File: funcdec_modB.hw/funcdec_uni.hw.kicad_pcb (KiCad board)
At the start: 2 copper layers, 32 x 17.5 mm, 27 parts, among them J1 Track2, J2 Track1, J3 PROG, J4 Functions, Q1 BSS138, Q2 AP2626, Q3 AP2626, Q4 AP2626, U1 AP2204K-5.0, U2 ATtiny1614-SS

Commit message: ack circuit correction
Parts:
- Q1: value BSS138 -> BC847
- R2: value 82R -> 150R
- R3: value 22k -> 15k
- R4: value 100R -> 10k
- moved Q1 0.13 mm to (39.8, 27.8)

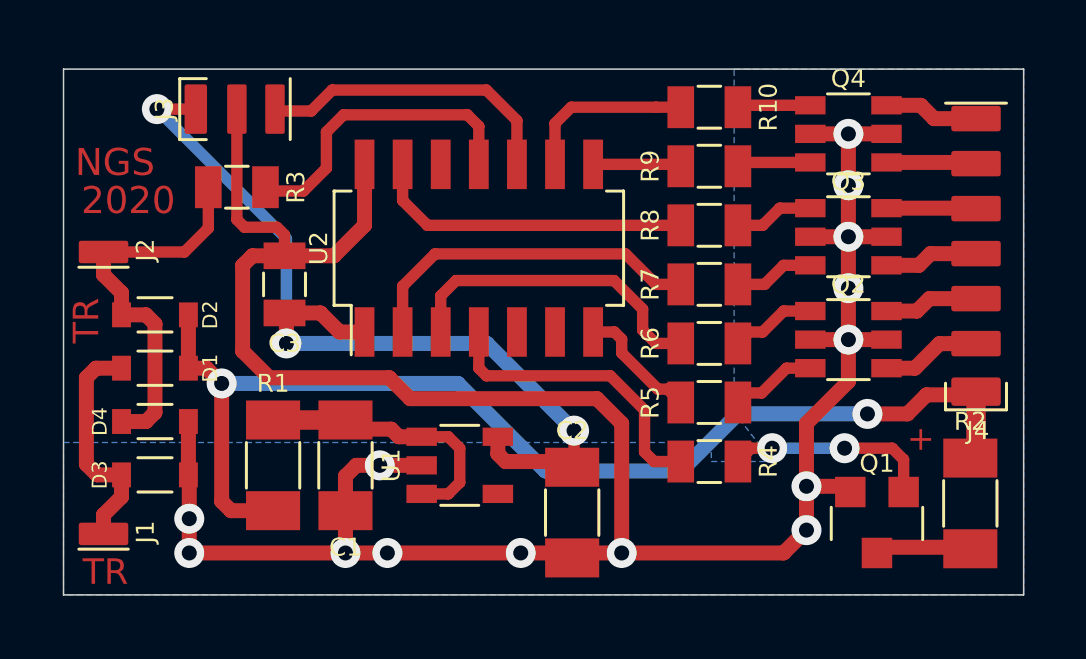
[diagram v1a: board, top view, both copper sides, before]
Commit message: corrections and file rename for manf
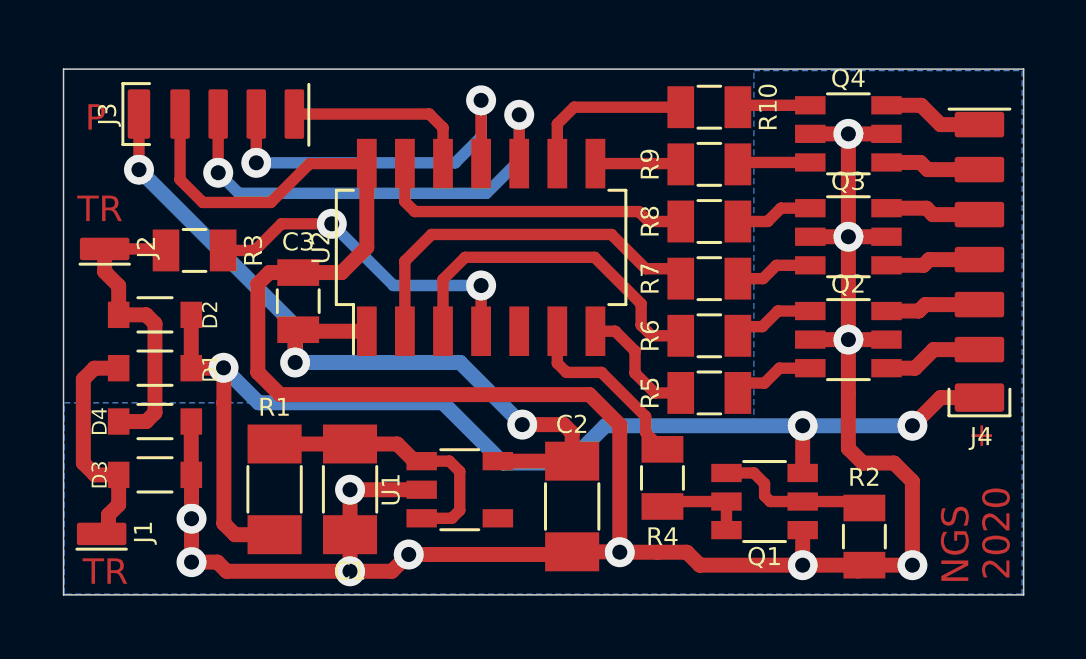
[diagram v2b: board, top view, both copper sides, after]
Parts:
- C1: value 10u -> 4.7u
- C2: value 22u -> 10u
- J1: value Track2 -> Padx1
- J2: value Track1 -> Padx1
- J3: value PROG -> Pad1.27x5; footprint NGS_Connectors_SMD:Array_1-27mm_1X3_SMD -> NGS_Connectors_SMD:Array_1-27mm_1X5_SMD
- J4: value Functions -> Pad1.5x7
- Q1: value BC847 -> BC817UE; footprint NGS Elements SMD:SOT23_HS -> NGS Elements SMD:SOT23-6_HS
- R2: value 150R -> 8R2; footprint NGS Elements SMD:SMD_1206_HS -> NGS Elements SMD:SMD_0805_HS
- moved Q1 3.81 mm to (36.1, 27.1), turned to 90 degrees
- moved R2 3.70 mm to (39.4, 28.3)
- moved R3 2.54 mm to (17.1, 18.7)
- moved R4 1.65 mm to (32.7, 26.3), turned to 90 degrees
- moved C1 0.81 mm to (22.3, 26.7)
- moved U1 0.81 mm to (25.9, 26.7)
- moved R1 0.80 mm to (19.7, 26.7)
- moved C3 0.72 mm to (20.5, 20.4), turned to 270 degrees
- moved J3 0.65 mm to (17.9, 14.2)
- moved R5 0.32 mm to (34.2, 23.5)
- moved R6 0.25 mm to (34.2, 21.6)
- moved J4 0.23 mm to (43.2, 19.1)
- moved C2 0.20 mm to (29.7, 27.3)
- moved R7 0.19 mm to (34.2, 19.7)
- moved R8 0.13 mm to (34.2, 17.8)
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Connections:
- C3 pad 1: VCC -> GND
- C3 pad 2: GND -> VCC
- Q1 pad 1: Net-(Q1-Pad1) -> GND
- Q1 pad 2: GND -> Net-(Q1-Pad2)
- Q1 pad 3: Net-(Q1-Pad3) -> Net-(D1-Pad1)
- R2 pad 1: Net-(D1-Pad1) -> Net-(Q1-Pad2)
- R2 pad 2: Net-(Q1-Pad3) -> GND
- R4 pad 1: Net-(Q1-Pad1) -> Net-(Q1-Pad5)
- U2 pad 11: /DCC -> Net-(J3-Pad4)
- U2 pad 12: Net-(U2-Pad12) -> Net-(J3-Pad5)
- U2 pad 4: /ACK -> /DCC
- U2 pad 6: Net-(U2-Pad6) -> /ACK
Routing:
- net Net-(J3-Pad4): track 0.00 -> 12.8 mm, vias 0 -> 2
- net GND: track 87.1 -> 95.7 mm, vias 14 -> 11
- net Net-(Q1-Pad1): track 6.75 -> 0.00 mm, vias 2 -> 0
- net Net-(J3-Pad5): track 0.00 -> 6.34 mm
- net Net-(J3-Pad3): track 10.3 -> 15.9 mm, vias 0 -> 2
- net Net-(Q1-Pad2): track 0.00 -> 5.32 mm
- net /ACK: track 10.0 -> 6.07 mm
- net Net-(Q1-Pad5): track 0.00 -> 3.15 mm
- net Net-(Q1-Pad3): track 3.13 -> 0.00 mm
- net Net-(D2-Pad2): track 13.0 -> 10.1 mm
- net VCC: track 30.2 -> 27.5 mm
- net /DCC: track 9.85 -> 11.3 mm, vias 0 -> 2
- net /OUT3: track 11.7 -> 12.5 mm
- net /OUT2: track 10.7 -> 11.5 mm
- net Net-(D1-Pad1): track 38.6 -> 38.9 mm, vias 2 -> 3
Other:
- net class Default: clearance 0.305 -> 0.25
- rule trace_clearance: 0.305 -> 0.25
- board text added: "P"
